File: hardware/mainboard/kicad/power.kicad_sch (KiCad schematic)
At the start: 43 parts, among them J1 1S LiPo PCM / PH-2, J8 External cell NTC / hand sold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, Q2 AO3401A, SW1 MK-12C03-G015, U3 BQ24072TRGTR, U4 TPS63802DLAR

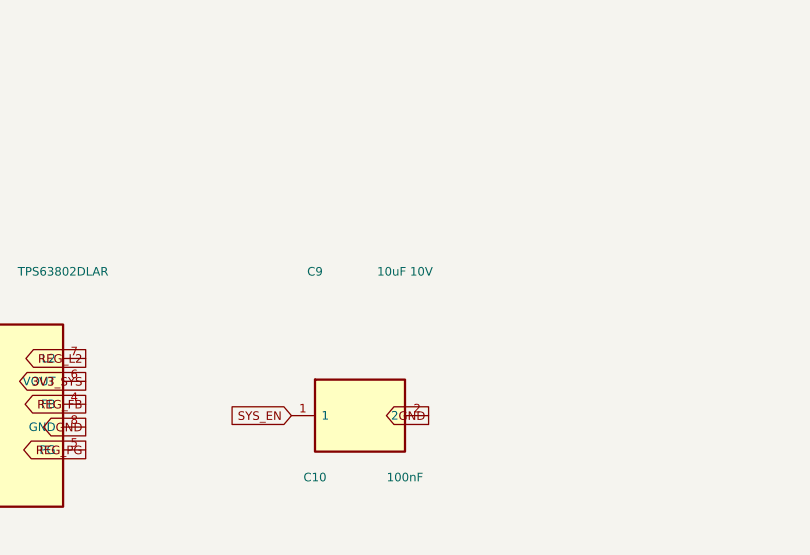
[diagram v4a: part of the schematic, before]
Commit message: R136: increase TPS63802 input C9 to22uF, preserve R135 geometry and enable immutable main/PR checks; NO FAB
Replace only four C9 properties in PCB/power source; all127 placements,438 pads,3707 copper items and nets remain unchanged. Review exact DC-bias scenarios and the0.95-to1.45mm local height change. Retain1140 R135 files, licensing and all history. Native local DRC/ERC/opens/parity0,23 scopes and8 rejection cases pass; actual immutable CI pending. Read existing supplier replies without outreach, manufacturing or purchasing.
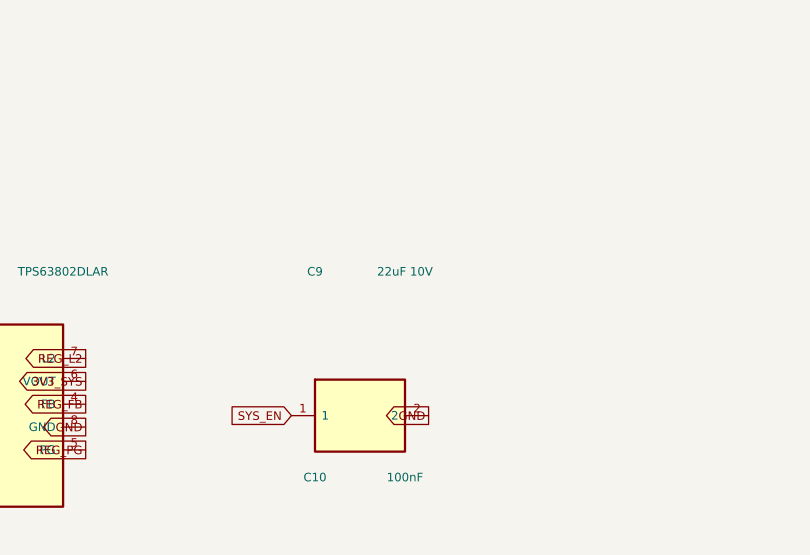
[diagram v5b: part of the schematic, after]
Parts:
- C9: value 10uF 10V -> 22uF 10V; MPN CC0805KKX5R6BB106 -> CC0805MKX5R6BB226
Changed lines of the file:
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@@
 	(symbol (lib_id "ENKU:C") (at 251.46 62.23 0) (unit 1) (exclude_from_sim no) (in_bom yes) (on_board yes) (dnp no)
 		(property "Reference" "C9" (at 246.46 46.23 0) (effects (font (size 0.95 0.95))))
-		(property "Value" "10uF 10V" (at 256.46 46.23 0) (effects (font (size 0.95 0.95))))
+		(property "Value" "22uF 10V" (at 256.46 46.23 0) (effects (font (size 0.95 0.95))))
 		(property "Footprint" "ENKU:C_CC0805_YAGEO_REFLOW_TRANSFER" (at 251.46 62.23 0) (effects (font (size 0.95 0.95)) (hide yes)))
-		(property "Datasheet" "https://yageogroup.com/download/specsheet/CC0805KKX5R6BB106" (at 251.46 62.23 0) (effects (font (size 0.95 0.95)) (hide yes)))
-		(property "Description" "10uF 10V" (at 251.46 62.23 0) (effects (font (size 0.95 0.95)) (hide yes)))
+		(property "Datasheet" "https://yageogroup.com/download/specsheet/CC0805MKX5R6BB226" (at 251.46 62.23 0) (effects (font (size 0.95 0.95)) (hide yes)))
+		(property "Description" "R136 TPS63802 input 22uF; modeled DC-bias margin; max height1.45mm; Ceff/fit qualification pending" (at 251.46 62.23 0) (effects (font (size 0.95 0.95)) (hide yes)))
 		(pin "1")
 		(pin "2")
 		(instances (project "enku-mainboard-r0.1" (path "/10000000-0000-4000-8000-000000000001/70000000-0000-4000-8000-000000000194" (reference "C9") (unit 1))))
-		(property "MPN" "CC0805KKX5R6BB106" (at 0 0 0) (effects (font (size .8 .8)) (hide yes)))
+		(property "MPN" "CC0805MKX5R6BB226" (at 0 0 0) (effects (font (size .8 .8)) (hide yes)))
 		(property "Manufacturer" "Yageo" (at 0 0 0) (effects (font (size .8 .8)) (hide yes)))
 		(property "Assembly" "FIT" (at 0 0 0) (effects (font (size .8 .8)) (hide yes)))
